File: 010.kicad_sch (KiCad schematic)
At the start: 21 parts, among them U1 AM6232ASCGHAALWR, U4 SN74LV1T125DBVR, X1 32.768kHz 12.5pF, X2 25MHz

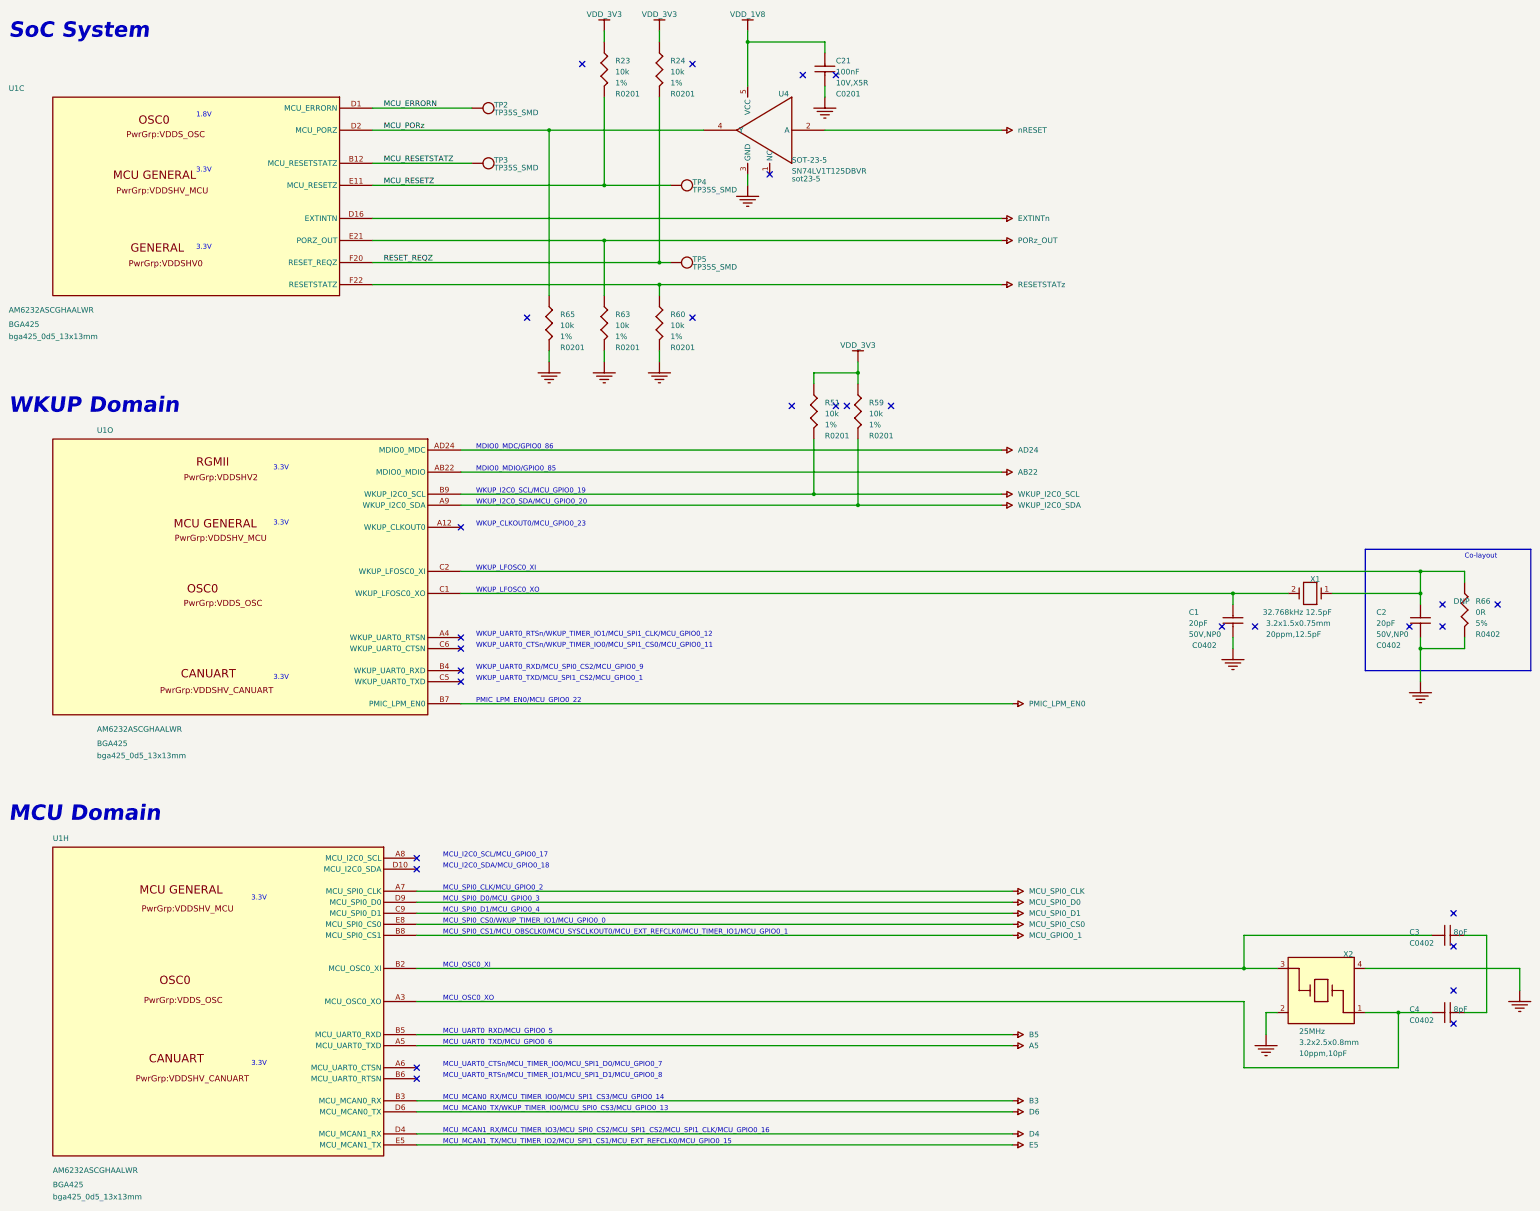
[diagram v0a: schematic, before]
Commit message: Remove rando NCs added during conversion
Also a little tidying.

TODO: check junctions that may be missing. Noticed a few obvious ones
and corrected them already.

Signed-off-by: Michael Welling <mwelling79@gmail.com>
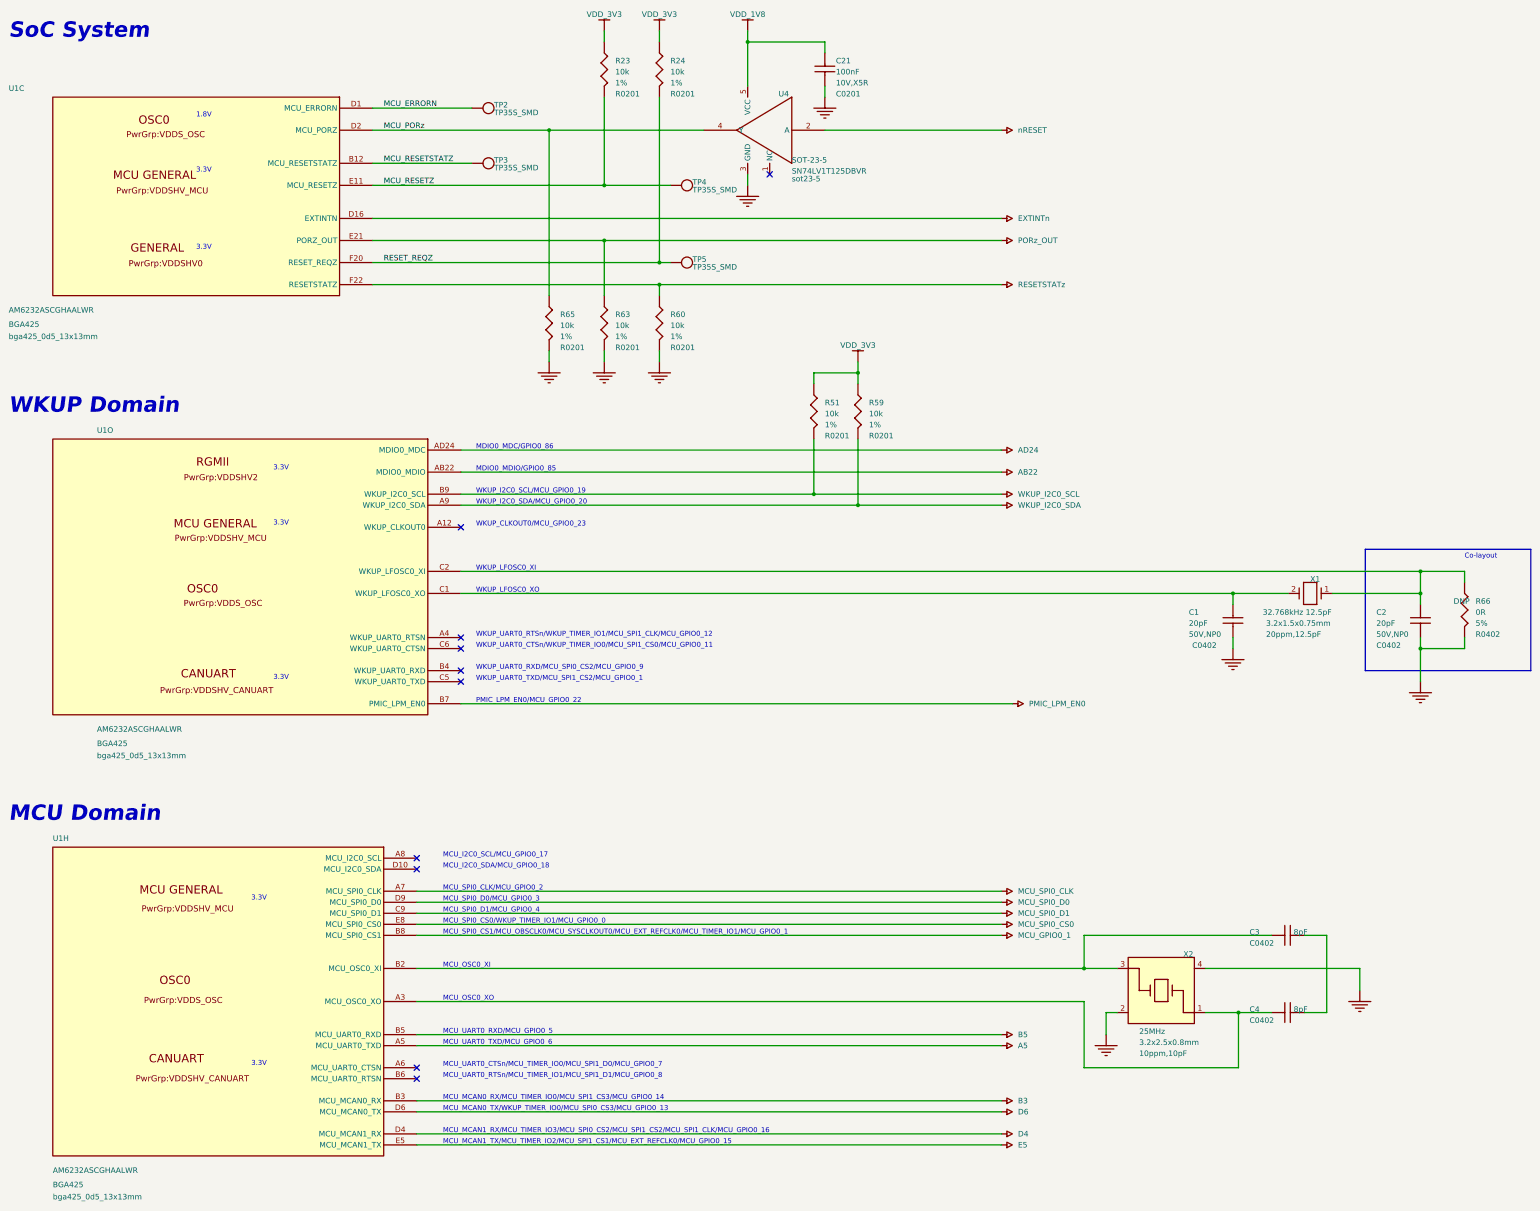
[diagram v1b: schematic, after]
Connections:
- no-connect marks 30 -> 10
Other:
- moved on the sheet: C3, C4, X2

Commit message: Another round of cleansing fire
Signed-off-by: Michael Welling <mwelling79@gmail.com>
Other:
- moved on the sheet: C3, C4, U1H, X2

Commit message: Moar fixes
Mostly missing junctions flagged in review on discord.

Signed-off-by: Michael Welling <mwelling79@gmail.com>
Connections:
- net GND: now also C3.2, C4.2
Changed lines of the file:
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@@
+	)
+	(junction
+		(at 318.77 228.6)
+		(diameter 0)
+		(color 0 0 0 0)
 	)
 	(junction
@@
 	(wire
 		(pts
-			(xy 290.83 228.6) (xy 326.39 228.6)
-		)
-		(stroke
-			(width 0)
-			(type default)
-		)
-	)
-	(wire
-		(pts
-			(xy 318.77 238.76) (xy 318.77 220.98)
+			(xy 290.83 228.6) (xy 318.77 228.6)
+		)
+		(stroke
+			(width 0)
+			(type default)
+		)
+	)
+	(wire
+		(pts
+			(xy 318.77 238.76) (xy 318.77 228.6)
 		)
 		(stroke
@@
 	(wire
 		(pts
+			(xy 318.77 228.6) (xy 318.77 220.98)
+		)
+		(stroke
+			(width 0)
+			(type default)
+		)
+	)
+	(wire
+		(pts
 			(xy 297.18 149.86) (xy 297.18 147.32)
 		)
@@
 		)
 		(stroke
+			(width 0)
+			(type default)
+		)
+	)
+	(wire
+		(pts
+			(xy 318.77 228.6) (xy 326.39 228.6)
+		)
+		(stroke
